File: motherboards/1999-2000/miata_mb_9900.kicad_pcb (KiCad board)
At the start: 2 copper layers, 154 x 161.5 mm, 28 parts, among them J1 TE 176122-6, J2 LSU 4.9, J3 IAT, J4 USB-C, J5 AUX 2x8, U2 MPX5700AP, U4 USBLC6-2SC6

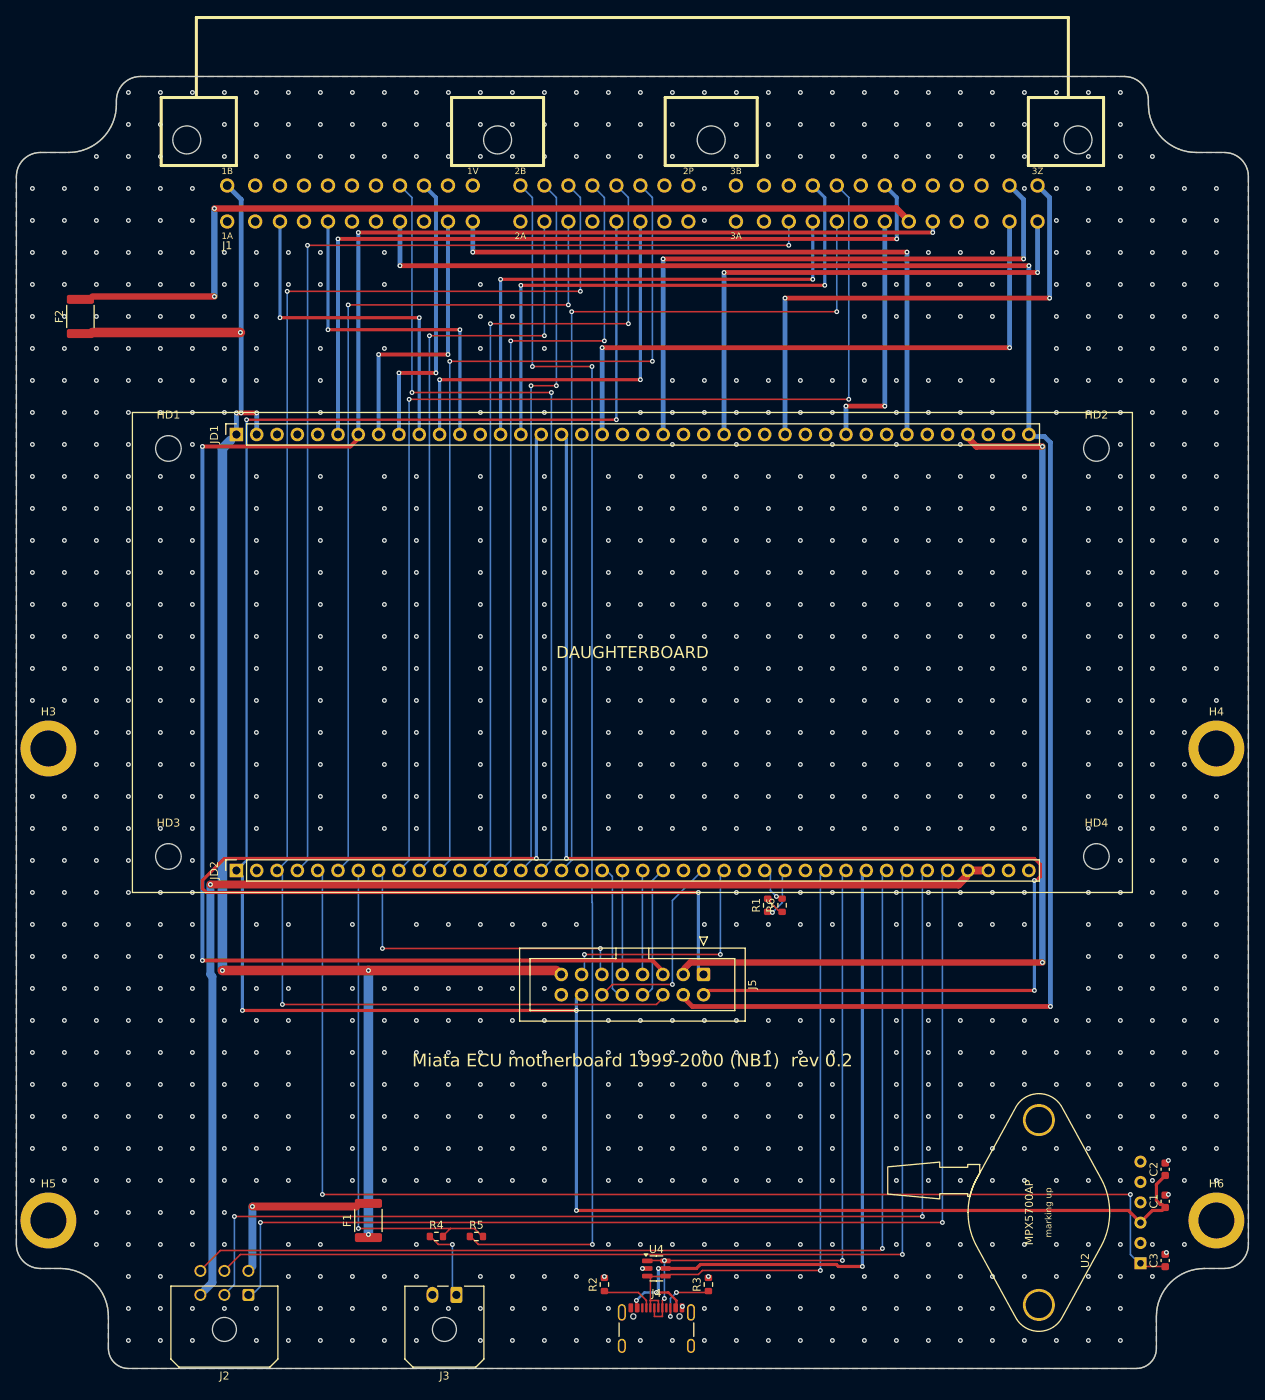
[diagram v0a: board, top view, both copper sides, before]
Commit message: IAT source jumper on every motherboard; wideband MCU flashed through the main MCU
- motherboards (1989-93 / 1994-95 rev 0.5, 1996-97 / 1999-2000 / 2001-05
  rev 0.3): the R4/R5 0R links are replaced by JP1, a 1x3 2.54 mm header with
  a removable shunt (STOCK = harness sensor, EXT = IAT connector, default)
- daughterboard rev 0.4: USART3 (PD8/PD9) to the STM32F042's ROM-bootloader
  USART1 (PA9/PA10), plus PD10 -> its BOOT0 and PD11 -> its NRST, so both
  MCUs can be flashed over the one USB-C port (rusEFI support to be written;
  SWD pads kept as a fallback)
- scripts: schematic check now also catches nets split across sheets;
  motherboard project template bundled
- README: flashing and IAT sections

Co-Authored-By: Claude Opus 5.5 <noreply@anthropic.com>
Claude-Session: https://claude.ai/code/session_012UFcA8PhPqkqYxcgEjD2n9
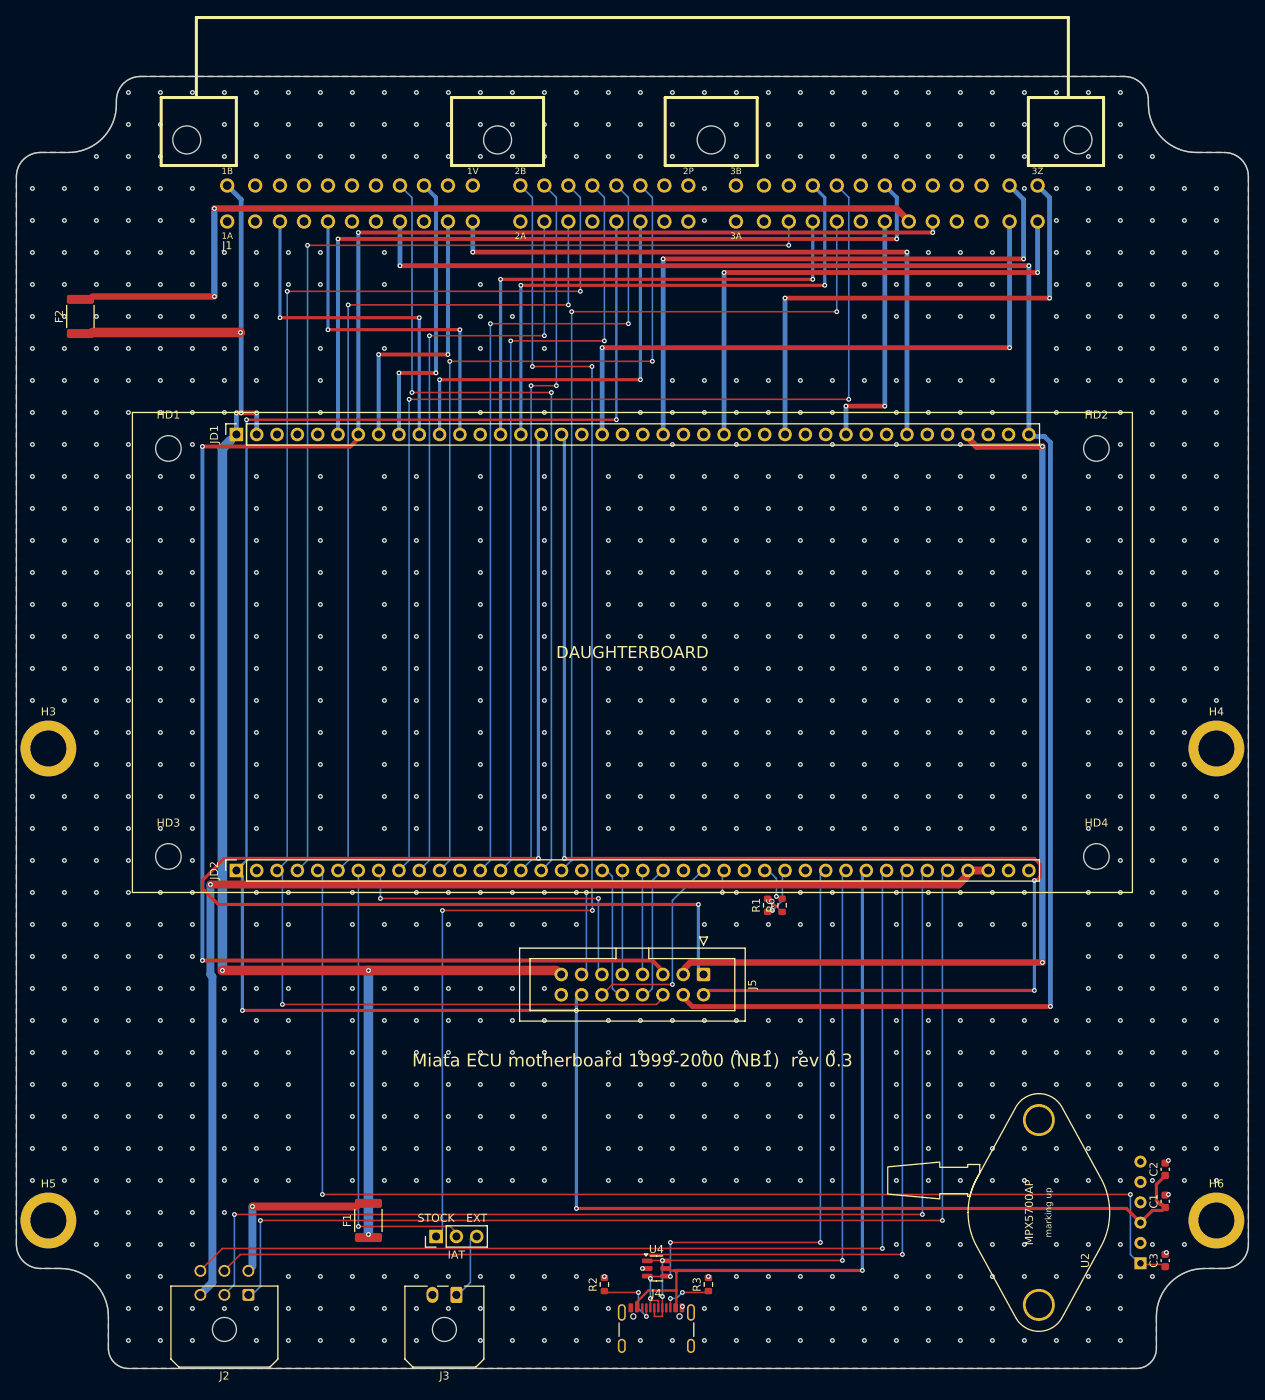
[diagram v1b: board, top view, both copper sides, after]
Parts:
- removed R4, R5: 0R, Resistor_SMD:R_0603_1608Metric
- added JP1: IAT SEL, Connector_PinHeader_2.54mm:PinHeader_1x03_P2.54mm_Vertical, F.Cu at (152.5, 195.0)
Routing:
- net IN_IAT: track 60.6 -> 56.0 mm
- net /LSU, MAP, IAT, USB, AUX/USB_CC1: track 5.91 -> 8.16 mm, vias 0 -> 2
- net /LSU, MAP, IAT, USB, AUX/USB_CC2: track 7.81 -> 5.56 mm
- net HARN_IAT: track 155.8 -> 157.4 mm, vias 3 -> 4
- net /LSU, MAP, IAT, USB, AUX/IAT_EXT: track 8.31 -> 6.91 mm, vias 1 -> 0
- net OUT_IGN3: track 168.1 -> 167.2 mm
- net USB_DM: track 74.2 -> 74.8 mm, vias 1 -> 5
- net USB_VBUS: track 83.5 -> 83.7 mm, vias 4 -> 1
- net GND: vias 1054 -> 1052
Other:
- board text added: "EXT"
- board text added: "IAT"
- board text added: "Miata ECU motherboard 1999-2000 (NB1) rev 0.3"
- board text added: "STOCK"
- board text removed: "Miata ECU motherboard 1999-2000 (NB1) rev 0.2"

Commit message: Rev 0.5 daughterboard, rev 0.6 1989-93/1994-95 motherboards: review fixes
Daughterboard rev 0.5:
- SN74LVC4245A drives the eight AUIPS2041 low sides at 5 V; output enable pulled
  off (R71) until the firmware enables it on PA8.
- BOOT1 pull-down (R72); hall input clamps D13/D14.
- ULN2003 COM to an SMAJ33A TVS (D11) instead of +12V: no key-off back-feed,
  no conduction in a 35 V load dump.
- Logic supply: D7/D8 -> 0.5 A PTC F1 -> SMAJ33A D12; C16 50 V, SS36 D9, C59.
- Tach stays an output.

Motherboards:
- Idle/VVT freewheel diodes, 4.7k switch pull-up options (not fitted),
  AUX VBAT PTC on all years.
- 1989-93 rev 0.6: two drivers per injector wire (0R links), SMCJ40A clamps.
- 2001-05: J1 3B tied to 3A.

Firmware: low-side enable (inverted open drain, forced writes, off during
configuration changes), unused control pins parked with pull-down, 1989-93
batch on all four outputs, VBATT offset noted.

Verification: 18/18 board tests, 119/119 harness check, circuit sims
20 OK / 3 CHECK / 6 REF / 0 FAIL, flash sim 9/9, firmware and bootloader
build; all boards 0 unconnected, 0 clearance errors.

Co-Authored-By: Claude Opus 5.5 <noreply@anthropic.com>
Claude-Session: https://claude.ai/code/session_012UFcA8PhPqkqYxcgEjD2n9
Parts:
- added D1: SS34, Diode_SMD:D_SMA, F.Cu at (203.7, 102.0)
- added F4: 0.5A hold, Fuse:Fuse_1206_3216Metric, F.Cu at (198.0, 163.0)
- added R20: 4.7k, Resistor_SMD:R_0603_1608Metric, F.Cu at (163.1, 144.0)
- added R21: 4.7k, Resistor_SMD:R_0603_1608Metric, F.Cu at (165.6, 144.0)
- added R22: 4.7k, Resistor_SMD:R_0603_1608Metric, F.Cu at (168.1, 144.0)
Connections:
- J5 pad 15: VBAT_IN -> /LSU, MAP, IAT, USB, AUX/AUX_VBAT
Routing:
- net IAC_12V: track 112.9 -> 192.5 mm, vias 2 -> 5
- net VBAT_IN: track 197.0 -> 266.6 mm, vias 7 -> 9
- net /LSU, MAP, IAT, USB, AUX/AUX_VBAT: track 0.00 -> 37.8 mm, vias 0 -> 3
- net OUT_IGN4: track 169.0 -> 173.5 mm, vias 3 -> 2
- net OUT_IACV: track 31.5 -> 34.7 mm, vias 2 -> 3
- net IN_MAP: track 151.2 -> 148.7 mm, vias 2 -> 1
- net OUT_IGN3: track 167.2 -> 165.8 mm
- net IN_SW2: track 104.2 -> 105.4 mm, vias 2 -> 3
- net IN_SW3: track 114.8 -> 115.8 mm, vias 2 -> 3
- net IN_SW1: track 89.9 -> 90.7 mm, vias 2 -> 3
- net OUT_MAINRLY: track 239.9 -> 240.5 mm, vias 4 -> 5
- net USB_DM: track 74.8 -> 74.2 mm, vias 5 -> 1
- net OUT_ALT: track 223.9 -> 224.3 mm, vias 3 -> 4
- net OUT_BOOST: track 118.9 -> 118.5 mm, vias 2 -> 3
- net USB_VBUS: track 83.7 -> 83.9 mm, vias 1 -> 4
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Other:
- board text added: "Miata ECU motherboard 1999-2000 (NB1) rev 0.4"
- board text removed: "Miata ECU motherboard 1999-2000 (NB1) rev 0.3"
